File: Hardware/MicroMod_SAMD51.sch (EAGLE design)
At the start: 30 parts, among them J2 MICROMOD-2222, U1 W25QXX128MBIT-6X5-NO_CENTER, U2 ATSAMD51J20A-A, Y1 32.768kHz

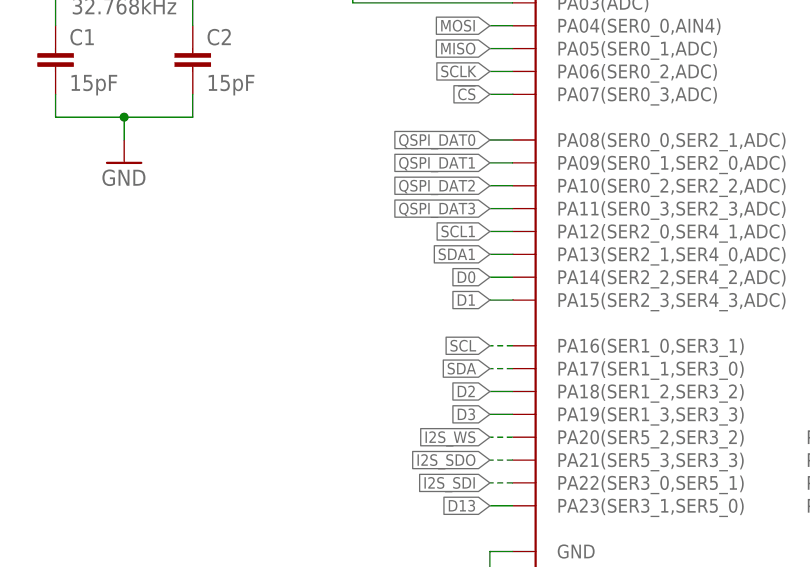
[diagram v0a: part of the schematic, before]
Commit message: Modifies about half of the variant.cpp file for
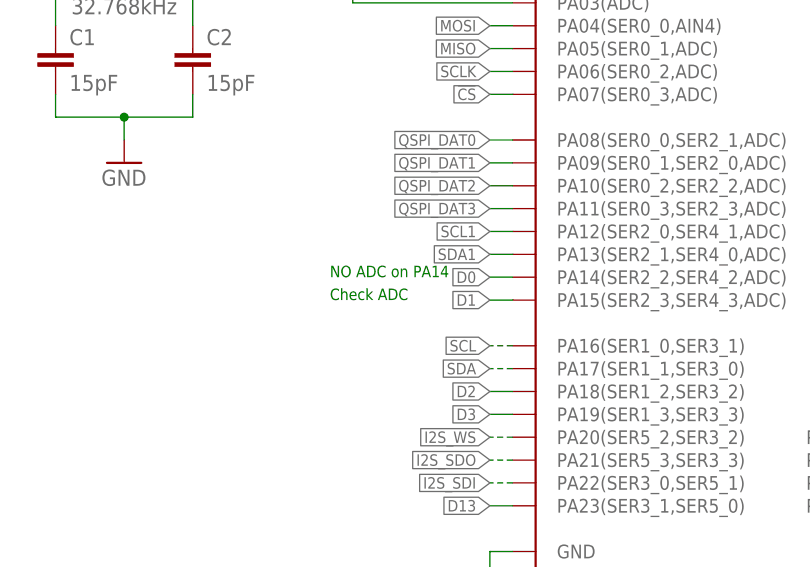
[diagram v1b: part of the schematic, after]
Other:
- note added: "Check ADC"
- note added: "NO ADC on PA14"
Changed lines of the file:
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@@
 <text x="285.496" y="242.062" size="1.778" layer="97">0.65uA Leakage
 0.3V drop at 10mA</text>
+<text x="68.58" y="198.12" size="1.27" layer="91">NO ADC on PA14</text>
+<text x="68.58" y="195.58" size="1.27" layer="91">Check ADC</text>
 </plain>
 <instances>

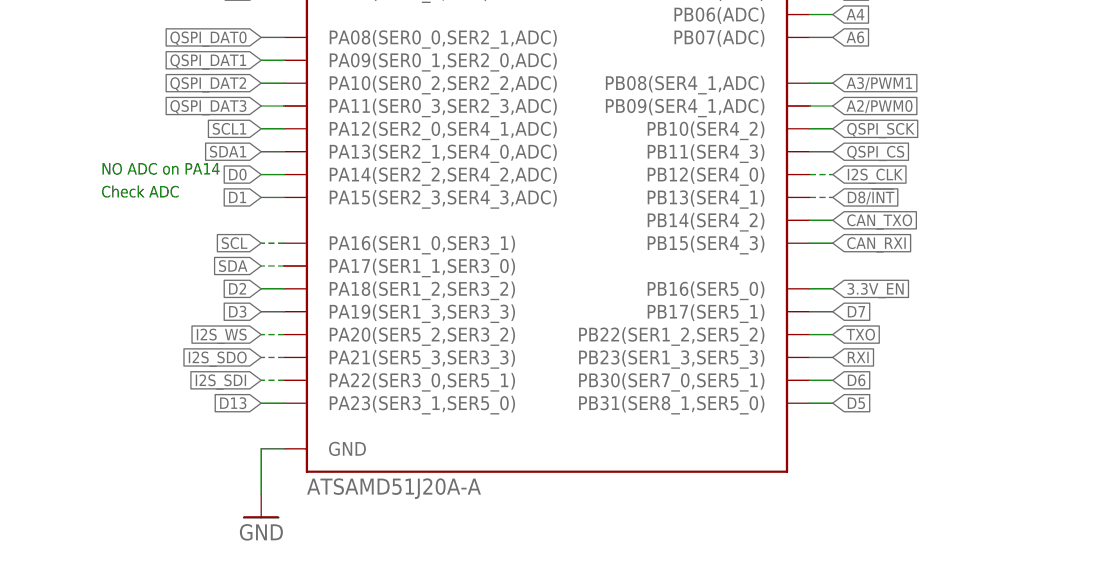
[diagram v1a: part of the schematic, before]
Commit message: Fills pin definitions  in variants, fixes I2S and D13 which were swapped (I2S Bus was crossing IOSETs)
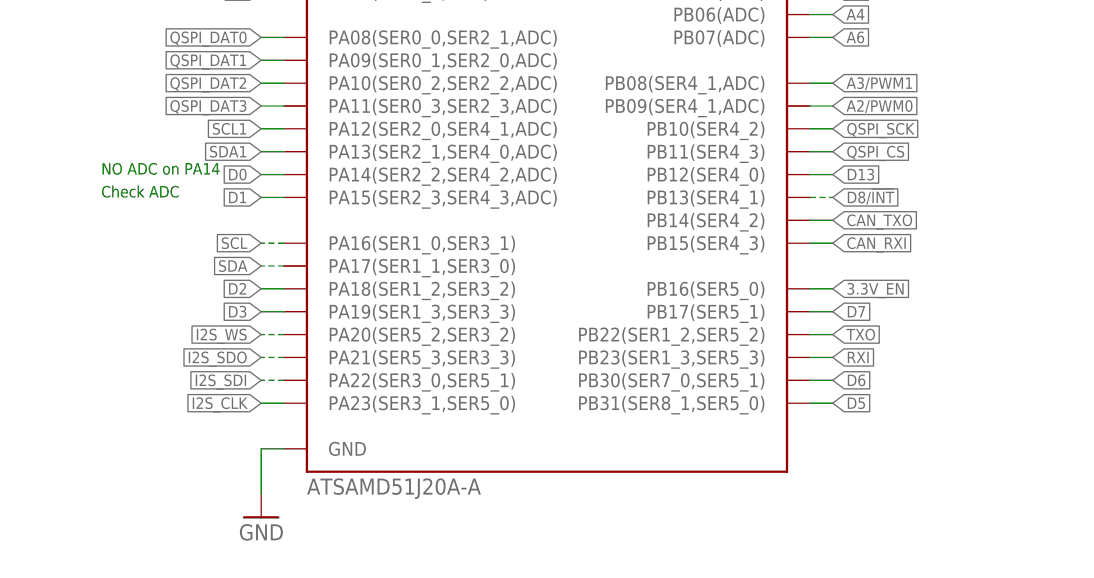
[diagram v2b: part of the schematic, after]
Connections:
- net D13: now also U2.PB12(SER4_0); no longer U2.PA23(SER3_1,SER5_0)
- net I2S_CLK: now also U2.PA23(SER3_1,SER5_0); no longer U2.PB12(SER4_0)
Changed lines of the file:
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@@
 </segment>
 <segment>
-<pinref part="U2" gate="G$1" pin="PA23(SER3_1,SER5_0)"/>
-<wire x1="88.9" y1="172.72" x2="86.36" y2="172.72" width="0.1524" layer="91"/>
-<label x="86.36" y="172.72" size="1.27" layer="95" rot="R180" xref="yes"/>
+<pinref part="U2" gate="G$1" pin="PB12(SER4_0)"/>
+<wire x1="147.32" y1="198.12" x2="149.86" y2="198.12" width="0.1524" layer="91"/>
+<label x="149.86" y="198.12" size="1.27" layer="95" xref="yes"/>
 </segment>
 </net>
@@
 <net name="I2S_CLK" class="0">
 <segment>
-<wire x1="147.32" y1="198.12" x2="149.86" y2="198.12" width="0.1524" layer="91" style="dashdot"/>
-<label x="149.86" y="198.12" size="1.27" layer="95" xref="yes"/>
-<pinref part="U2" gate="G$1" pin="PB12(SER4_0)"/>
-</segment>
-<segment>
 <wire x1="299.72" y1="170.18" x2="297.18" y2="170.18" width="0.1524" layer="91"/>
 <label x="297.18" y="170.18" size="1.27" layer="95" rot="R180" xref="yes"/>
 <pinref part="J2" gate="J1" pin="AUD_BCLK"/>
 </segment>
-</net>
+<segment>
+<pinref part="U2" gate="G$1" pin="PA23(SER3_1,SER5_0)"/>
+<wire x1="88.9" y1="172.72" x2="86.36" y2="172.72" width="0.1524" layer="91"/>
+<label x="86.36" y="172.72" size="1.27" layer="95" rot="R180" xref="yes"/>
+</segment>
+</net>

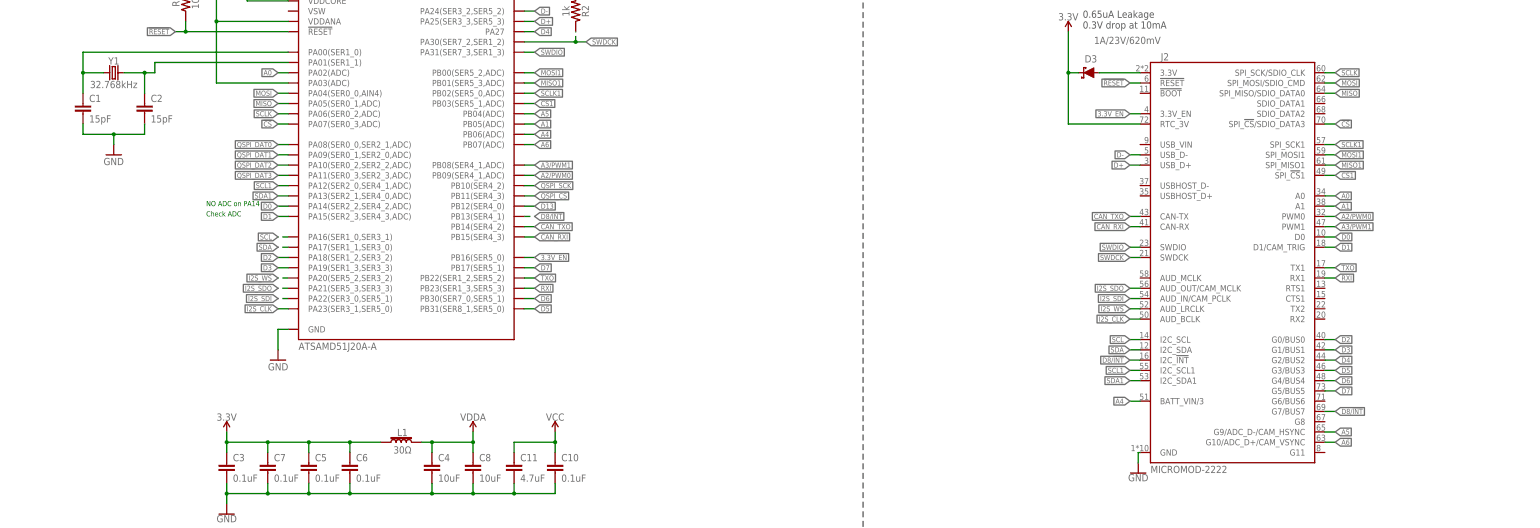
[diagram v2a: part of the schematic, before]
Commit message: Changes so that SPI and I2C work
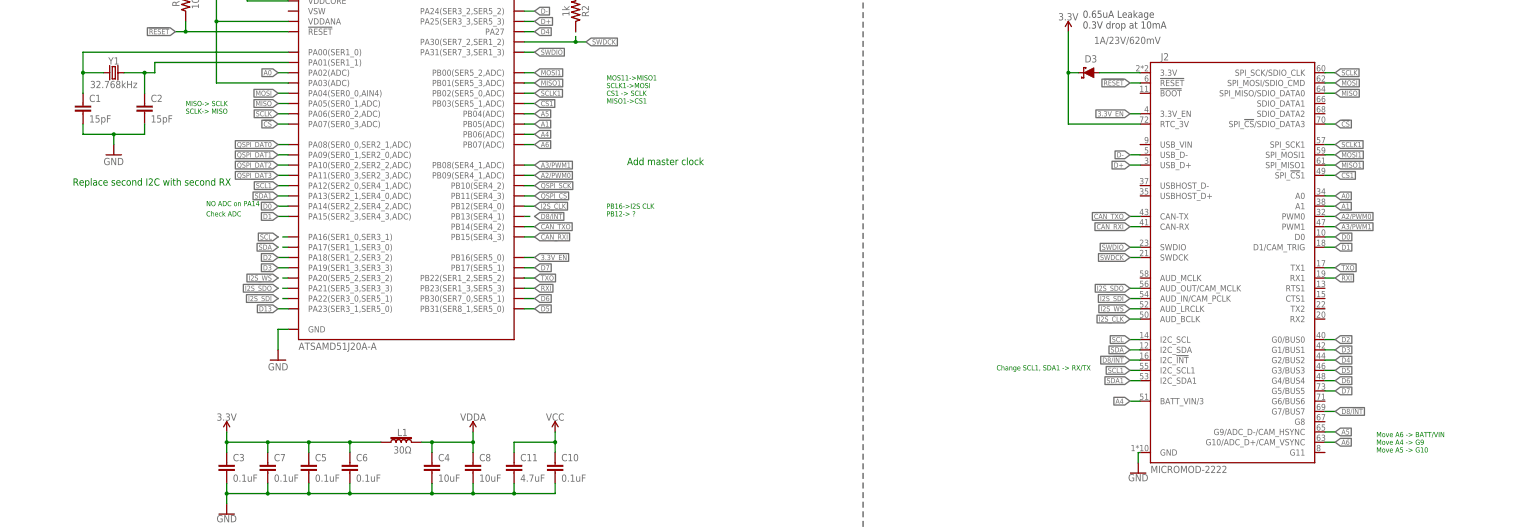
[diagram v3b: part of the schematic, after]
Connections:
- net D13: now also U2.PA23(SER3_1,SER5_0); no longer U2.PB12(SER4_0)
- net I2S_CLK: now also U2.PB12(SER4_0); no longer U2.PA23(SER3_1,SER5_0)
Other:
- note added: "Add master clock"
- note added: "Change SCL1, SDA1 -> RX/TX"
- note added: "MISO-> SCLK SCLK-> MISO"
- note added: "MOS11->MISO1 SCLK1->MOSI CS1 -> SCLK MISO1->CS1"
- note added: "Move A6 -> BATT/VIN Move A4 -> G9 Move A5 -> G10"
- note added: "PB16->I2S CLK PB12-> ?"
- note added: "Replace second I2C with second RX"
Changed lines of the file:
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@@
 <text x="68.58" y="198.12" size="1.27" layer="91">NO ADC on PA14</text>
 <text x="68.58" y="195.58" size="1.27" layer="91">Check ADC</text>
+<text x="358.14" y="137.16" size="1.27" layer="91">Move A6 -&gt; BATT/VIN
+Move A4 -&gt; G9
+Move A5 -&gt; G10</text>
+<text x="264.16" y="157.48" size="1.27" layer="91">Change SCL1, SDA1 -&gt; RX/TX</text>
+<text x="167.64" y="223.52" size="1.27" layer="91">MOS11-&gt;MISO1
+SCLK1-&gt;MOSI
+CS1 -&gt; SCLK
+MISO1-&gt;CS1</text>
+<text x="63.5" y="220.98" size="1.27" layer="91">MISO-&gt; SCLK
+SCLK-&gt; MISO
+</text>
+<text x="172.72" y="208.28" size="1.778" layer="91">Add master clock</text>
+<text x="35.56" y="203.2" size="1.778" layer="91">Replace second I2C with second RX</text>
+<text x="167.64" y="195.58" size="1.27" layer="91">PB16-&gt;I2S CLK
+PB12-&gt; ?</text>
 </plain>
 <instances>
@@
 </segment>
 <segment>
-<pinref part="U2" gate="G$1" pin="PB12(SER4_0)"/>
-<wire x1="147.32" y1="198.12" x2="149.86" y2="198.12" width="0.1524" layer="91"/>
-<label x="149.86" y="198.12" size="1.27" layer="95" xref="yes"/>
+<pinref part="U2" gate="G$1" pin="PA23(SER3_1,SER5_0)"/>
+<wire x1="86.36" y1="172.72" x2="88.9" y2="172.72" width="0.1524" layer="91"/>
+<label x="86.36" y="172.72" size="1.27" layer="95" rot="R180" xref="yes"/>
 </segment>
 </net>
@@
 </segment>
 <segment>
-<pinref part="U2" gate="G$1" pin="PA23(SER3_1,SER5_0)"/>
-<wire x1="88.9" y1="172.72" x2="86.36" y2="172.72" width="0.1524" layer="91"/>
-<label x="86.36" y="172.72" size="1.27" layer="95" rot="R180" xref="yes"/>
-</segment>
-</net>
+<pinref part="U2" gate="G$1" pin="PB12(SER4_0)"/>
+<wire x1="147.32" y1="198.12" x2="149.86" y2="198.12" width="0.1524" layer="91"/>
+<label x="149.86" y="198.12" size="1.27" layer="95" xref="yes"/>
+</segment>
+</net>

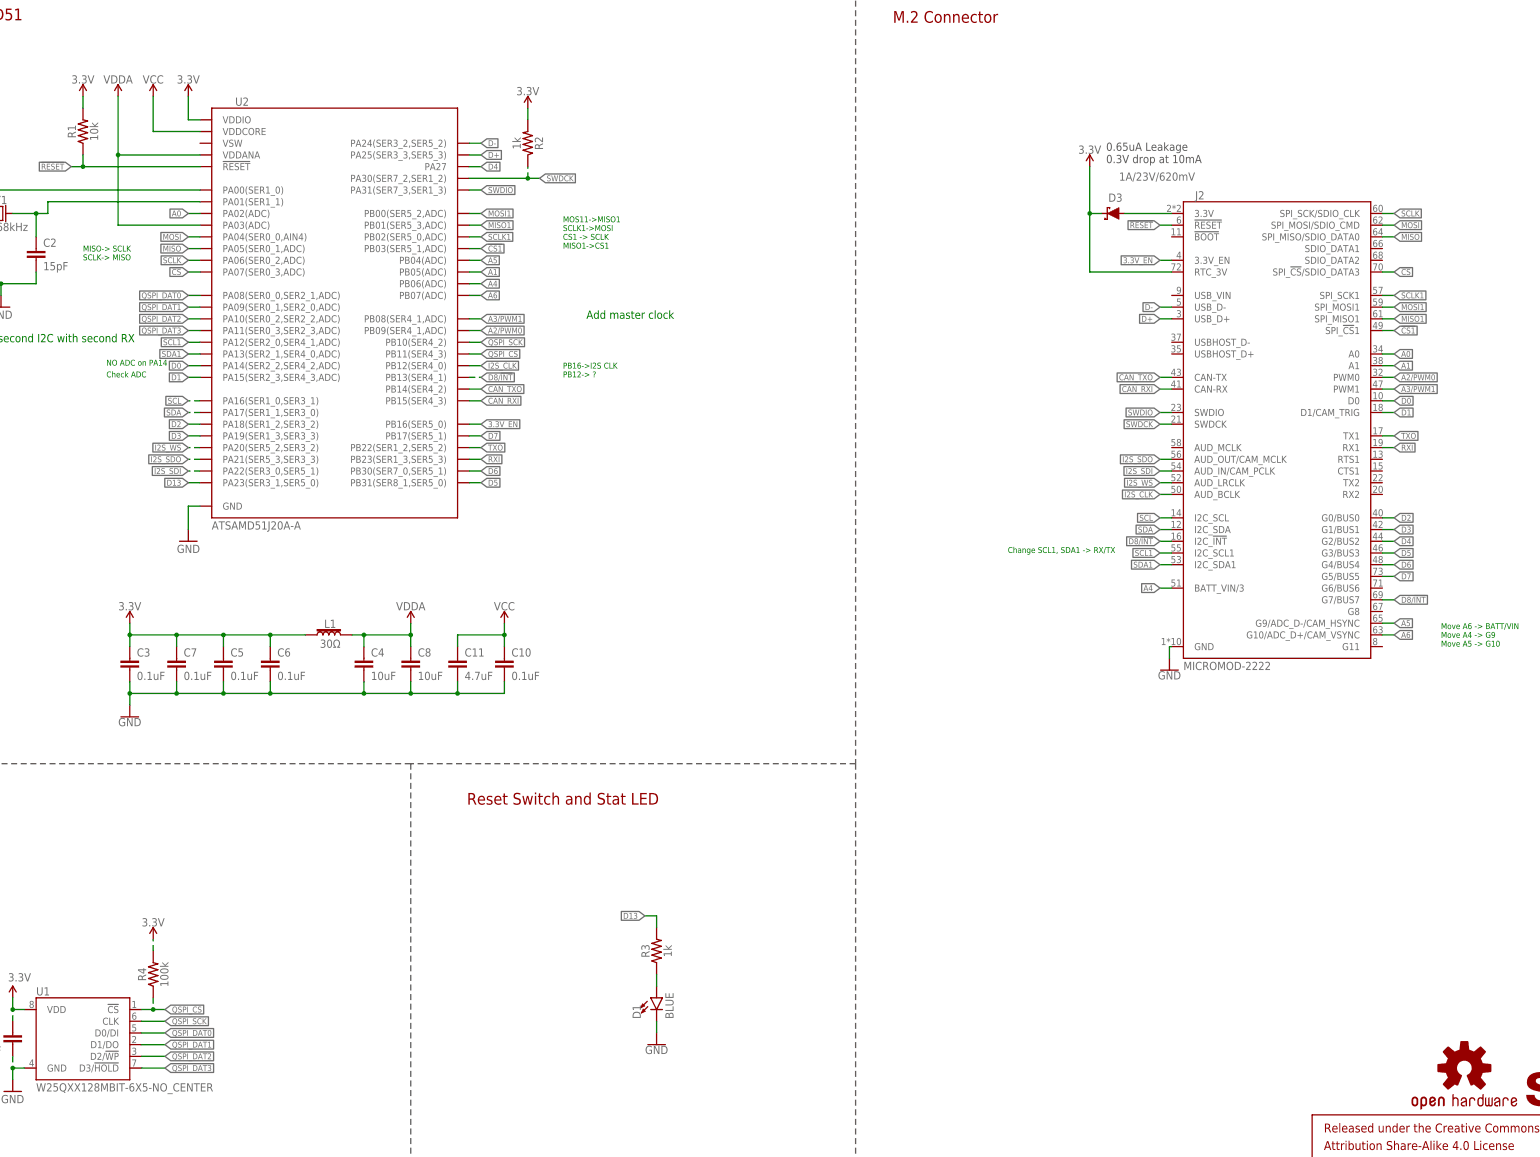
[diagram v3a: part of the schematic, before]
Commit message: Various testing elements in Variant files regarding Serial1 and Serial2
* Changes old SPI naming convention to new one
* Moves some pins around for more thought out layout (more details to come)
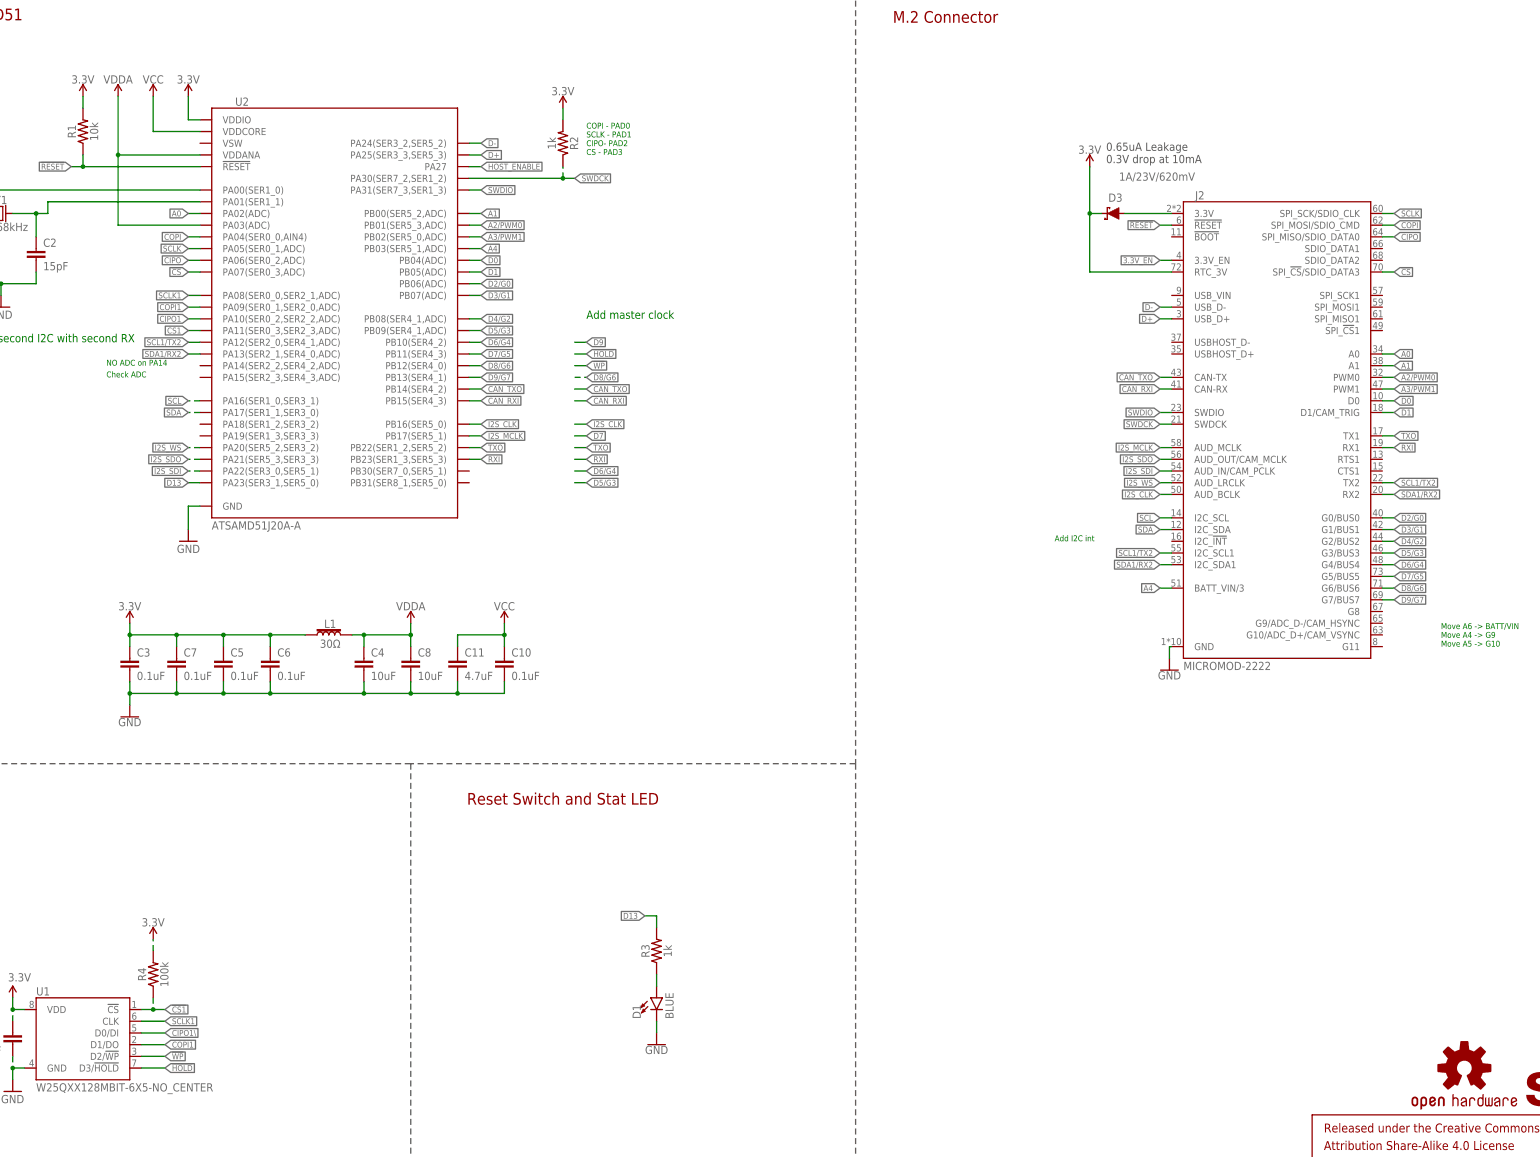
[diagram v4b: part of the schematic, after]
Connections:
- net MOSI renamed COPI
- net QSPI_DAT1 renamed COPI1
- removed net !CS1: J2.SPI_!CS!1, U2.PB03(SER5_1,ADC)
- removed net A5: J2.G9/ADC_D-/CAM_HSYNC, U2.PB04(ADC)
- removed net A6: J2.G10/ADC_D+/CAM_VSYNC, U2.PB07(ADC)
- removed net D2: J2.G0/BUS0, U2.PA18(SER1_2,SER3_2)
- removed net D3: J2.G1/BUS1, U2.PA19(SER1_3,SER3_3)
- removed net D4: J2.G2/BUS2, U2.PA27
- removed net D5: J2.G3/BUS3, U2.PB31(SER8_1,SER5_0)
- removed net D6: J2.G4/BUS4, U2.PB30(SER7_0,SER5_1)
- removed net D7: J2.G5/BUS5, U2.PB17(SER5_1)
- removed net D8/!INT: J2.G7/BUS7, J2.I2C_!INT!, U2.PB13(SER4_1)
- removed net MISO: J2.SPI_MISO/SDIO_DATA0, U2.PA05(SER0_1,ADC)
- removed net MISO1: J2.SPI_MISO1, U2.PB01(SER5_3,ADC)
- removed net MOSI1: J2.SPI_MOSI1, U2.PB00(SER5_2,ADC)
- removed net QSPI_CS: R4.1, U1.!CS!, U2.PB11(SER4_3)
- removed net QSPI_DAT0: U1.D0/DI, U2.PA08(SER0_0,SER2_1,ADC)
- removed net QSPI_DAT2: U1.D2/!WP!, U2.PA10(SER0_2,SER2_2,ADC)
- removed net QSPI_DAT3: U1.D3/!HOLD!, U2.PA11(SER0_3,SER2_3,ADC)
- removed net QSPI_SCK: U1.CLK, U2.PB10(SER4_2)
- removed net SCL1: J2.I2C_SCL1, U2.PA12(SER2_0,SER4_1,ADC)
- removed net SDA1: J2.I2C_SDA1, U2.PA13(SER2_1,SER4_0,ADC)
- new net !CS1!: R4.1, U1.!CS!
- new net !HOLD!: U1.D3/!HOLD!
- new net !WP!: U1.D2/!WP!
- new net CIPO: J2.SPI_MISO/SDIO_DATA0, U2.PA06(SER0_2,ADC)
- new net CIPO1: U2.PA10(SER0_2,SER2_2,ADC)
- new net CIPO1\: U1.D0/DI
- new net CS1: U2.PA11(SER0_3,SER2_3,ADC)
- new net D2/G0: J2.G0/BUS0, U2.PB06(ADC)
- new net D3/G1: J2.G1/BUS1, U2.PB07(ADC)
- new net D4/G2: J2.G2/BUS2, U2.PB08(SER4_1,ADC)
- new net D5/G3: J2.G3/BUS3, U2.PB09(SER4_1,ADC)
- new net D6/G4: J2.G4/BUS4, U2.PB10(SER4_2)
- new net D7/G5: J2.G5/BUS5, U2.PB11(SER4_3)
- new net D8/G6: J2.G6/BUS6, U2.PB12(SER4_0)
- new net D9/G7: J2.G7/BUS7, U2.PB13(SER4_1)
- new net HOST_ENABLE: U2.PA27
- new net I2S_MCLK: J2.AUD_MCLK, U2.PB17(SER5_1)
- new net SCL1/TX2: J2.I2C_SCL1, J2.TX2, U2.PA12(SER2_0,SER4_1,ADC)
- new net SDA1/RX2: J2.I2C_SDA1, J2.RX2, U2.PA13(SER2_1,SER4_0,ADC)
- net 3.3V_EN: no longer U2.PB16(SER5_0)
- net A1: now also U2.PB00(SER5_2,ADC); no longer U2.PB05(ADC)
- net A2/PWM0: now also U2.PB01(SER5_3,ADC); no longer U2.PB09(SER4_1,ADC)
- net A3/PWM1: now also U2.PB02(SER5_0,ADC); no longer U2.PB08(SER4_1,ADC)
- net A4: now also U2.PB03(SER5_1,ADC); no longer U2.PB06(ADC)
- net D0: now also U2.PB04(ADC); no longer U2.PA14(SER2_2,SER4_2,ADC)
- net D1: now also U2.PB05(ADC); no longer U2.PA15(SER2_3,SER4_3,ADC)
- net I2S_CLK: now also U2.PB16(SER5_0); no longer U2.PB12(SER4_0)
- net SCLK: now also U2.PA05(SER0_1,ADC); no longer U2.PA06(SER0_2,ADC)
- net SCLK1: now also U1.CLK, U2.PA08(SER0_0,SER2_1,ADC); no longer J2.SPI_SCK1, U2.PB02(SER5_0,ADC)
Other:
- note added: "Add I2C int"
- note added: "COPI - PAD0 SCLK - PAD1 CIPO- PAD2 CS - PAD3"
- note removed: "Change SCL1, SDA1 -> RX/TX"
- note removed: "MISO-> SCLK SCLK-> MISO"
- note removed: "MOS11->MISO1 SCLK1->MOSI CS1 -> SCLK MISO1->CS1"
- note removed: "PB16->I2S CLK PB12-> ?"
- moved on the sheet: R2
